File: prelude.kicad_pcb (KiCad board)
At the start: 2 copper layers, 80 x 60 mm, 41 parts, among them J1 CONN_01X50, J2 USB_C, J3 Conn_01x04, J4 Conn_01x08, SW1 SW_Push, U1 LM3671MF-3.3, U2 STM32F411RETx, U3 AP5724, Y1 16MHz

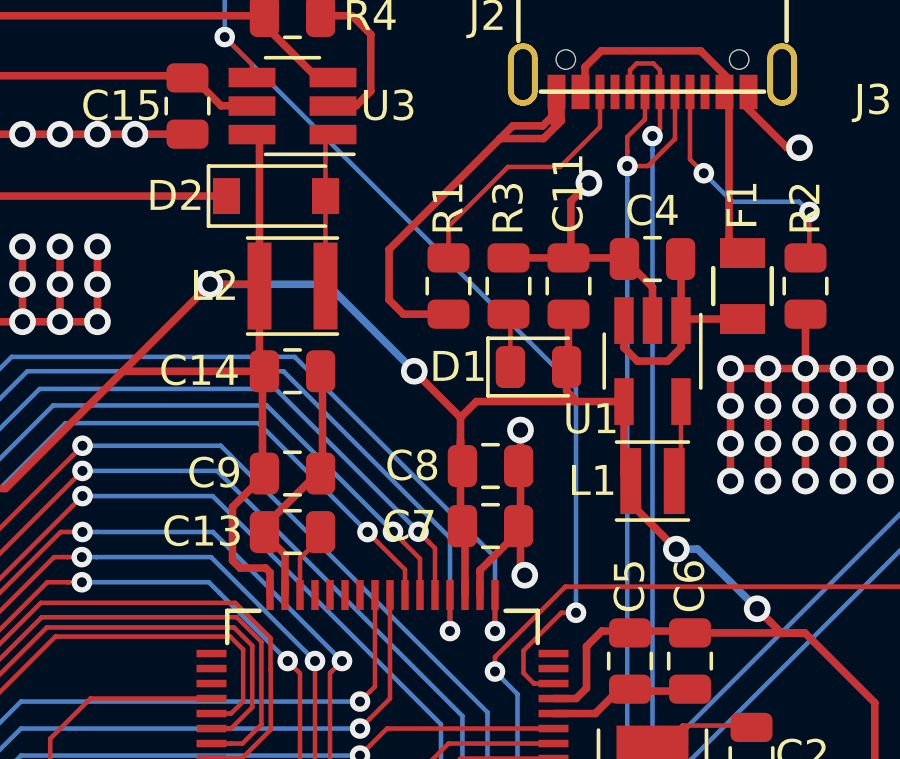
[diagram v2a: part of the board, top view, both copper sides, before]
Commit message: Replaces inductors with HandSoldering versions, recalculated fills, still need to adjust vias
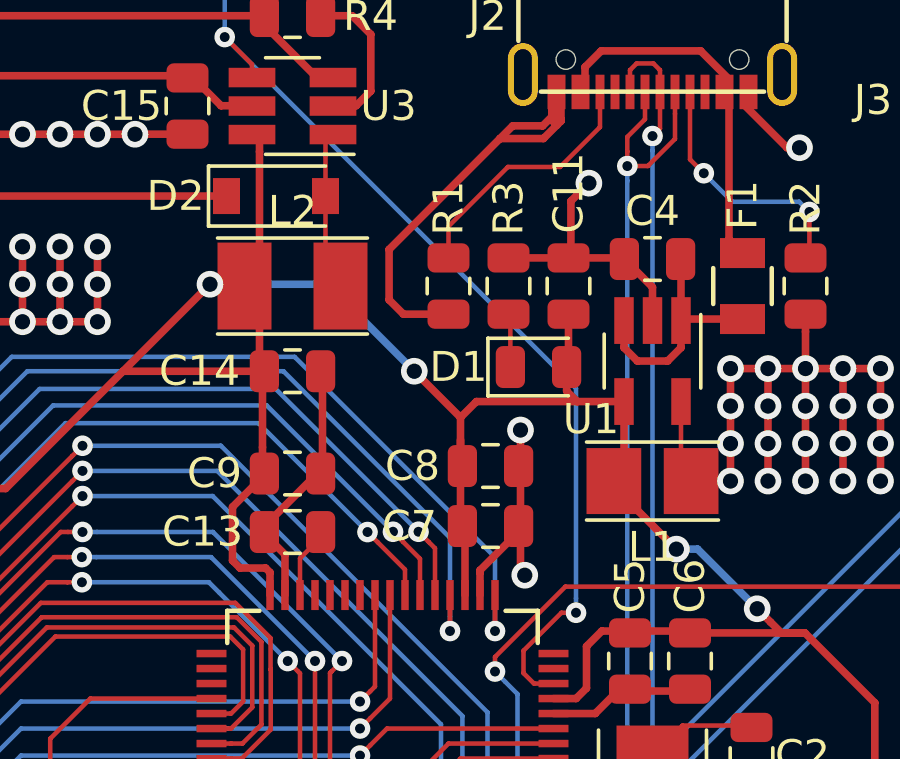
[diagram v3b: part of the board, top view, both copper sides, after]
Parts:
- L1: footprint Inductor_SMD:L_Taiyo-Yuden_NR-24xx -> Inductor_SMD:L_Taiyo-Yuden_NR-24xx_HandSoldering
- L2: footprint Inductor_SMD:L_Taiyo-Yuden_NR-30xx -> Inductor_SMD:L_Taiyo-Yuden_NR-30xx_HandSoldering
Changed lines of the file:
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@@
-    )
-  )
-  (module Inductor_SMD:L_Taiyo-Yuden_NR-24xx (layer Top)
-    (at 175 60.5 180)
-    (descr "Inductor, Taiyo Yuden, NR series, Taiyo-Yuden_NR-24xx, 2.4mmx2.4mm")
-    (tags "inductor taiyo-yuden nr smd")
-    (attr smd)
-    (fp_text reference L1 (at 2 0 180) (layer F.SilkS)
-      (effects (font (size 1 1) (thickness 0.15)))
-    )
-    (fp_text value 2.2uH (at 0 2.7 180) (layer F.Fab)
-      (effects (font (size 1 1) (thickness 0.15)))
-    )
-    (fp_text user %R (at 0 0 180) (layer F.Fab)
-      (effects (font (size 0.5 0.5) (thickness 0.075)))
-    )
-    (fp_line (start -1.2 0) (end -1.2 -0.725) (layer F.Fab) (width 0.1))
-    (fp_line (start -1.2 -0.725) (end -0.725 -1.2) (layer F.Fab) (width 0.1))
-    (fp_line (start -0.725 -1.2) (end 0 -1.2) (layer F.Fab) (width 0.1))
-    (fp_line (start 1.2 0) (end 1.2 -0.725) (layer F.Fab) (width 0.1))
-    (fp_line (start 1.2 -0.725) (end 0.725 -1.2) (layer F.Fab) (width 0.1))
-    (fp_line (start 0.725 -1.2) (end 0 -1.2) (layer F.Fab) (width 0.1))
-    (fp_line (start 1.2 0) (end 1.2 0.725) (layer F.Fab) (width 0.1))
-    (fp_line (start 1.2 0.725) (end 0.725 1.2) (layer F.Fab) (width 0.1))
-    (fp_line (start 0.725 1.2) (end 0 1.2) (layer F.Fab) (width 0.1))
-    (fp_line (start -1.2 0) (end -1.2 0.725) (layer F.Fab) (width 0.1))
-    (fp_line (start -1.2 0.725) (end -0.725 1.2) (layer F.Fab) (width 0.1))
-    (fp_line (start -0.725 1.2) (end 0 1.2) (layer F.Fab) (width 0.1))
-    (fp_line (start -1.2 -1.3) (end 1.2 -1.3) (layer F.SilkS) (width 0.12))
-    (fp_line (start -1.2 1.3) (end 1.2 1.3) (layer F.SilkS) (width 0.12))
-    (fp_line (start -1.5 -1.5) (end -1.5 1.5) (layer F.CrtYd) (width 0.05))
-    (fp_line (start -1.5 1.5) (end 1.5 1.5) (layer F.CrtYd) (width 0.05))
-    (fp_line (start 1.5 1.5) (end 1.5 -1.5) (layer F.CrtYd) (width 0.05))
-    (fp_line (start 1.5 -1.5) (end -1.5 -1.5) (layer F.CrtYd) (width 0.05))
-    (pad 1 smd rect (at -0.725 0 180) (size 0.7 2.2) (layers Top F.Paste F.Mask)
-      (net 36 "Net-(L1-Pad1)"))
-    (pad 2 smd rect (at 0.725 0 180) (size 0.7 2.2) (layers Top F.Paste F.Mask)
-      (net 5 +3V3))
-    (model ${KISYS3DMOD}/Inductor_SMD.3dshapes/L_Taiyo-Yuden_NR-24xx.wrl
-      (at (xyz 0 0 0))
-      (scale (xyz 1 1 1))
-      (rotate (xyz 0 0 0))
-    )
-    (model C:/Github/3DModels/Inductor_Taiyo_Yuden_NR2412_original.step
-      (at (xyz 0 0 0))
-      (scale (xyz 1 1 1))
-      (rotate (xyz 0 0 0))
-    )
-  )
-  (module Inductor_SMD:L_Taiyo-Yuden_NR-30xx (layer Top)
-    (at 163 54)
-    (descr "Inductor, Taiyo Yuden, NR series, Taiyo-Yuden_NR-30xx, 3.0mmx3.0mm")
-    (tags "inductor taiyo-yuden nr smd")
-    (attr smd)
-    (fp_text reference L2 (at -2.6 0 180) (layer F.SilkS)
-      (effects (font (size 1 1) (thickness 0.15)))
-    )
-    (fp_text value 22uH (at 0 3) (layer F.Fab)
-      (effects (font (size 1 1) (thickness 0.15)))
-    )
-    (fp_text user %R (at 0 0) (layer F.Fab)
-      (effects (font (size 0.7 0.7) (thickness 0.105)))
-    )
-    (fp_line (start -1.5 0) (end -1.5 -0.95) (layer F.Fab) (width 0.1))
-    (fp_line (start -1.5 -0.95) (end -0.95 -1.5) (layer F.Fab) (width 0.1))
-    (fp_line (start -0.95 -1.5) (end 0 -1.5) (layer F.Fab) (width 0.1))
-    (fp_line (start 1.5 0) (end 1.5 -0.95) (layer F.Fab) (width 0.1))
-    (fp_line (start 1.5 -0.95) (end 0.95 -1.5) (layer F.Fab) (width 0.1))
-    (fp_line (start 0.95 -1.5) (end 0 -1.5) (layer F.Fab) (width 0.1))
-    (fp_line (start 1.5 0) (end 1.5 0.95) (layer F.Fab) (width 0.1))
-    (fp_line (start 1.5 0.95) (end 0.95 1.5) (layer F.Fab) (width 0.1))
-    (fp_line (start 0.95 1.5) (end 0 1.5) (layer F.Fab) (width 0.1))
-    (fp_line (start -1.5 0) (end -1.5 0.95) (layer F.Fab) (width 0.1))
-    (fp_line (start -1.5 0.95) (end -0.95 1.5) (layer F.Fab) (width 0.1))
-    (fp_line (start -0.95 1.5) (end 0 1.5) (layer F.Fab) (width 0.1))
-    (fp_line (start -1.5 -1.6) (end 1.5 -1.6) (layer F.SilkS) (width 0.12))
-    (fp_line (start -1.5 1.6) (end 1.5 1.6) (layer F.SilkS) (width 0.12))
-    (fp_line (start -1.8 -1.8) (end -1.8 1.8) (layer F.CrtYd) (width 0.05))
-    (fp_line (start -1.8 1.8) (end 1.8 1.8) (layer F.CrtYd) (width 0.05))
-    (fp_line (start 1.8 1.8) (end 1.8 -1.8) (layer F.CrtYd) (width 0.05))
-    (fp_line (start 1.8 -1.8) (end -1.8 -1.8) (layer F.CrtYd) (width 0.05))
-    (pad 1 smd rect (at -1.1 0) (size 0.8 2.9) (layers Top F.Paste F.Mask)
-      (net 5 +3V3))
-    (pad 2 smd rect (at 1.1 0) (size 0.8 2.9) (layers Top F.Paste F.Mask)
-      (net 8 "Net-(D2-Pad2)"))
-    (model ${KISYS3DMOD}/Inductor_SMD.3dshapes/L_Taiyo-Yuden_NR-30xx.wrl
-      (at (xyz 0 0 0))
-      (scale (xyz 1 1 1))
-      (rotate (xyz 0 0 0))
-    )
-    (model C:/Github/3DModels/Inductor_Taiyo_Yuden_NR3015_original.step
-      (at (xyz 0 0 0))
-      (scale (xyz 1 1 1))
-      (rotate (xyz 0 0 0))
     )
   )
@@
       (at (xyz 0 0 0))
       (scale (xyz 1 1 1))
+      (rotate (xyz 0 0 0))
+    )
+  )
+  (module Inductor_SMD:L_Taiyo-Yuden_NR-24xx_HandSoldering (layer Top)
+    (at 175 60.5 180)
+    (descr "Inductor, Taiyo Yuden, NR series, Taiyo-Yuden_NR-24xx, 2.4mmx2.4mm")
+    (tags "inductor taiyo-yuden nr smd")
+    (attr smd)
+    (fp_text reference L1 (at 0 -2.2 180) (layer F.SilkS)
+      (effects (font (size 1 1) (thickness 0.15)))
+    )
+    (fp_text value 2.2uH (at 0 2.7 180) (layer F.Fab)
+      (effects (font (size 1 1) (thickness 0.15)))
+    )
+    (fp_text user %R (at 0 0 180) (layer F.Fab)
+      (effects (font (size 0.5 0.5) (thickness 0.075)))
+    )
+    (fp_line (start -1.2 0) (end -1.2 -0.725) (layer F.Fab) (width 0.1))
+    (fp_line (start -1.2 -0.725) (end -0.725 -1.2) (layer F.Fab) (width 0.1))
+    (fp_line (start -0.725 -1.2) (end 0 -1.2) (layer F.Fab) (width 0.1))
+    (fp_line (start 1.2 0) (end 1.2 -0.725) (layer F.Fab) (width 0.1))
+    (fp_line (start 1.2 -0.725) (end 0.725 -1.2) (layer F.Fab) (width 0.1))
+    (fp_line (start 0.725 -1.2) (end 0 -1.2) (layer F.Fab) (width 0.1))
+    (fp_line (start 1.2 0) (end 1.2 0.725) (layer F.Fab) (width 0.1))
+    (fp_line (start 1.2 0.725) (end 0.725 1.2) (layer F.Fab) (width 0.1))
+    (fp_line (start 0.725 1.2) (end 0 1.2) (layer F.Fab) (width 0.1))
+    (fp_line (start -1.2 0) (end -1.2 0.725) (layer F.Fab) (width 0.1))
+    (fp_line (start -1.2 0.725) (end -0.725 1.2) (layer F.Fab) (width 0.1))
+    (fp_line (start -0.725 1.2) (end 0 1.2) (layer F.Fab) (width 0.1))
+    (fp_line (start -2.2 -1.3) (end 2.2 -1.3) (layer F.SilkS) (width 0.12))
+    (fp_line (start -2.2 1.3) (end 2.2 1.3) (layer F.SilkS) (width 0.12))
+    (fp_line (start -2.5 -1.5) (end -2.5 1.5) (layer F.CrtYd) (width 0.05))
+    (fp_line (start -2.5 1.5) (end 2.5 1.5) (layer F.CrtYd) (width 0.05))
+    (fp_line (start 2.5 1.5) (end 2.5 -1.5) (layer F.CrtYd) (width 0.05))
+    (fp_line (start 2.5 -1.5) (end -2.5 -1.5) (layer F.CrtYd) (width 0.05))
+    (pad 1 smd rect (at -1.2875 0 180) (size 1.825 2.2) (layers Top F.Paste F.Mask)
+      (net 36 "Net-(L1-Pad1)"))
+    (pad 2 smd rect (at 1.2875 0 180) (size 1.825 2.2) (layers Top F.Paste F.Mask)
+      (net 5 +3V3))
+    (model ${KISYS3DMOD}/Inductor_SMD.3dshapes/L_Taiyo-Yuden_NR-24xx.wrl
+      (at (xyz 0 0 0))
+      (scale (xyz 1 1 1))
+      (rotate (xyz 0 0 0))
+    )
+  )
+  (module Inductor_SMD:L_Taiyo-Yuden_NR-30xx_HandSoldering (layer Top)
+    (at 163 54)
+    (descr "Inductor, Taiyo Yuden, NR series, Taiyo-Yuden_NR-30xx, 3.0mmx3.0mm")
+    (tags "inductor taiyo-yuden nr smd")
+    (attr smd)
+    (fp_text reference L2 (at 0 -2.5) (layer F.SilkS)
+      (effects (font (size 1 1) (thickness 0.15)))
+    )
+    (fp_text value 22uH (at 0 3) (layer F.Fab)
+      (effects (font (size 1 1) (thickness 0.15)))
+    )
+    (fp_text user %R (at 0 0) (layer F.Fab)
+      (effects (font (size 0.7 0.7) (thickness 0.105)))
+    )
+    (fp_line (start -1.5 0) (end -1.5 -0.95) (layer F.Fab) (width 0.1))
+    (fp_line (start -1.5 -0.95) (end -0.95 -1.5) (layer F.Fab) (width 0.1))
+    (fp_line (start -0.95 -1.5) (end 0 -1.5) (layer F.Fab) (width 0.1))
+    (fp_line (start 1.5 0) (end 1.5 -0.95) (layer F.Fab) (width 0.1))
+    (fp_line (start 1.5 -0.95) (end 0.95 -1.5) (layer F.Fab) (width 0.1))
+    (fp_line (start 0.95 -1.5) (end 0 -1.5) (layer F.Fab) (width 0.1))
+    (fp_line (start 1.5 0) (end 1.5 0.95) (layer F.Fab) (width 0.1))
+    (fp_line (start 1.5 0.95) (end 0.95 1.5) (layer F.Fab) (width 0.1))
+    (fp_line (start 0.95 1.5) (end 0 1.5) (layer F.Fab) (width 0.1))
+    (fp_line (start -1.5 0) (end -1.5 0.95) (layer F.Fab) (width 0.1))
+    (fp_line (start -1.5 0.95) (end -0.95 1.5) (layer F.Fab) (width 0.1))
+    (fp_line (start -0.95 1.5) (end 0 1.5) (layer F.Fab) (width 0.1))
+    (fp_line (start -2.5 -1.6) (end 2.5 -1.6) (layer F.SilkS) (width 0.12))
+    (fp_line (start -2.5 1.6) (end 2.5 1.6) (layer F.SilkS) (width 0.12))
+    (fp_line (start -2.75 -1.8) (end -2.75 1.8) (layer F.CrtYd) (width 0.05))
+    (fp_line (start -2.75 1.8) (end 2.75 1.8) (layer F.CrtYd) (width 0.05))
+    (fp_line (start 2.75 1.8) (end 2.75 -1.8) (layer F.CrtYd) (width 0.05))
+    (fp_line (start 2.75 -1.8) (end -2.75 -1.8) (layer F.CrtYd) (width 0.05))
+    (pad 1 smd rect (at -1.6 0) (size 1.8 2.9) (layers Top F.Paste F.Mask)
+      (net 5 +3V3))
+    (pad 2 smd rect (at 1.6 0) (size 1.8 2.9) (layers Top F.Paste F.Mask)
+      (net 8 "Net-(D2-Pad2)"))
+    (model ${KISYS3DMOD}/Inductor_SMD.3dshapes/L_Taiyo-Yuden_NR-30xx.wrl
+      (at (xyz 0 0 0))
+      (scale (xyz 1 1 1))

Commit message: Adjusted vias and tracks with latest Inductor footprints (HandSoldering), removed row of vias
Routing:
- net GND: track 350.2 -> 345.2 mm, vias 224 -> 220
- net +3V3: track 206.7 -> 207.8 mm
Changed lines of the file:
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@@
     (thickness 1.6)
     (drawings 24)
-    (tracks 1102)
+    (tracks 1099)
     (zones 0)
     (modules 41)
@@
   (via (at 180.1 56.75) (size 0.889) (drill 0.508) (layers Top Bottom) (net 2))
   (via (at 178.85 56.75) (size 0.889) (drill 0.508) (layers Top Bottom) (net 2))
-  (via (at 177.6 56.75) (size 0.889) (drill 0.508) (layers Top Bottom) (net 2))
   (via (at 178.85 58) (size 0.889) (drill 0.508) (layers Top Bottom) (net 2))
-  (via (at 177.6 58) (size 0.889) (drill 0.508) (layers Top Bottom) (net 2))
   (via (at 178.85 59.25) (size 0.889) (drill 0.508) (layers Top Bottom) (net 2))
-  (via (at 177.6 59.25) (size 0.889) (drill 0.508) (layers Top Bottom) (net 2))
   (via (at 178.85 60.5) (size 0.889) (drill 0.508) (layers Top Bottom) (net 2))
-  (via (at 177.6 60.5) (size 0.889) (drill 0.508) (layers Top Bottom) (net 2))
   (via (at 181.35 56.75) (size 0.889) (drill 0.508) (layers Top Bottom) (net 2))
-  (via (at 182.6 56.75) (size 0.889) (drill 0.508) (layers Top Bottom) (net 2))
   (via (at 180.1 58) (size 0.889) (drill 0.508) (layers Top Bottom) (net 2))
   (via (at 181.35 58) (size 0.889) (drill 0.508) (layers Top Bottom) (net 2))
-  (via (at 182.6 58) (size 0.889) (drill 0.508) (layers Top Bottom) (net 2))
   (via (at 180.1 59.25) (size 0.889) (drill 0.508) (layers Top Bottom) (net 2))
   (via (at 181.35 59.25) (size 0.889) (drill 0.508) (layers Top Bottom) (net 2))
-  (via (at 182.6 59.25) (size 0.889) (drill 0.508) (layers Top Bottom) (net 2))
   (via (at 180.1 60.5) (size 0.889) (drill 0.508) (layers Top Bottom) (net 2))
   (via (at 181.35 60.5) (size 0.889) (drill 0.508) (layers Top Bottom) (net 2))
-  (via (at 182.6 60.5) (size 0.889) (drill 0.508) (layers Top Bottom) (net 2))
   (segment (start 149.732222 59.75) (end 148.865 59.75) (width 0.254) (layer Top) (net 2))
   (segment (start 150.25 55.19) (end 150.25 59.232222) (width 0.254) (layer Top) (net 2))
@@
   (segment (start 149 52.69) (end 149 53.94) (width 0.254) (layer Top) (net 2))
   (segment (start 149 53.94) (end 149 55.19) (width 0.254) (layer Top) (net 2))
-  (segment (start 178.85 56.75) (end 177.6 56.75) (width 0.254) (layer Top) (net 2))
   (segment (start 178.85 56.75) (end 180.1 56.75) (width 0.254) (layer Top) (net 2))
   (segment (start 180.1 56.75) (end 181.35 56.75) (width 0.254) (layer Top) (net 2))
-  (segment (start 181.35 56.75) (end 182.6 56.75) (width 0.254) (layer Top) (net 2))
-  (segment (start 182.6 56.75) (end 182.6 58) (width 0.254) (layer Top) (net 2))
   (segment (start 181.35 56.75) (end 181.35 58) (width 0.254) (layer Top) (net 2))
   (segment (start 181.35 58) (end 181.35 59.25) (width 0.254) (layer Top) (net 2))
@@
   (segment (start 178.85 58) (end 178.85 59.25) (width 0.254) (layer Top) (net 2))
   (segment (start 178.85 59.25) (end 178.85 60.5) (width 0.254) (layer Top) (net 2))
-  (segment (start 177.6 56.75) (end 177.6 58) (width 0.254) (layer Top) (net 2))
-  (segment (start 177.6 58) (end 177.6 59.25) (width 0.254) (layer Top) (net 2))
-  (segment (start 177.6 59.25) (end 177.6 60.5) (width 0.254) (layer Top) (net 2))
-  (segment (start 182.6 58) (end 182.6 59.25) (width 0.254) (layer Top) (net 2))
-  (segment (start 182.6 59.25) (end 182.6 60.5) (width 0.254) (layer Top) (net 2))
   (via (at 180.2975 71.8375) (size 0.889) (drill 0.508) (layers Top Bottom) (net 2))
   (segment (start 180.2975 71.8375) (end 180.2975 70.5875) (width 0.254) (layer Top) (net 2))
@@
   (segment (start 170.4 85.7) (end 170.4 86.654) (width 0.254) (layer Top) (net 2))
   (segment (start 170.4 86.654) (end 170.796 87.05) (width 0.254) (layer Top) (net 2))
+  (segment (start 182.6 59.25) (end 182.6 60.5) (width 0.254) (layer Top) (net 2))
+  (segment (start 181.35 56.75) (end 182.6 56.75) (width 0.254) (layer Top) (net 2))
+  (segment (start 182.6 58) (end 182.6 59.25) (width 0.254) (layer Top) (net 2))
+  (segment (start 182.6 56.75) (end 182.6 58) (width 0.254) (layer Top) (net 2))
+  (via (at 182.6 59.25) (size 0.889) (drill 0.508) (layers Top Bottom) (net 2))
+  (via (at 182.6 60.5) (size 0.889) (drill 0.508) (layers Top Bottom) (net 2))
+  (via (at 182.6 58) (size 0.889) (drill 0.508) (layers Top Bottom) (net 2))
+  (via (at 182.6 56.75) (size 0.889) (drill 0.508) (layers Top Bottom) (net 2))
   (segment (start 178 68.65) (end 176 68.65) (width 0.1524) (layer Top) (net 3))
   (segment (start 176 68.65) (end 175 69.65) (width 0.1524) (layer Top) (net 3))
@@
   (segment (start 174.05 60.275) (end 174.275 60.5) (width 0.254) (layer Top) (net 5))
   (segment (start 174.05 57.85) (end 174.05 60.275) (width 0.254) (layer Top) (net 5))
-  (segment (start 164.16 53.94) (end 167.06 56.84) (width 0.254) (layer Bottom) (net 5))
-  (via (at 160.25 53.94) (size 0.889) (drill 0.508) (layers Top Bottom) (net 5))
-  (segment (start 153.44 60.75) (end 160.25 53.94) (width 0.254) (layer Top) (net 5))
-  (segment (start 148.865 60.75) (end 153.44 60.75) (width 0.254) (layer Top) (net 5))
-  (segment (start 157.35 56.84) (end 161.98 56.84) (width 0.254) (layer Top) (net 5))
-  (segment (start 161.84 53.94) (end 161.9 54) (width 0.254) (layer Top) (net 5))
-  (segment (start 160.25 53.94) (end 161.84 53.94) (width 0.254) (layer Top) (net 5))
-  (segment (start 160.25 53.94) (end 164.16 53.94) (width 0.254) (layer Bottom) (net 5))
   (segment (start 180.0825 65.5625) (end 179.29589 65.5625) (width 0.254) (layer Top) (net 5))
   (segment (start 179.29589 65.5625) (end 178.934499 65.201109) (width 0.254) (layer Top) (net 5))
@@
   (segment (start 156.578 97.028) (end 152.384 92.834) (width 0.254) (layer Top) (net 5))
   (segment (start 152.384 92.834) (end 152.384 84.696) (width 0.254) (layer Top) (net 5))
+  (via (at 159.749952 53.94) (size 0.889) (drill 0.508) (layers Top Bottom) (net 5))
+  (segment (start 160.378569 53.94) (end 159.749952 53.94) (width 0.254) (layer Top) (net 5))
+  (segment (start 161.9 54) (end 161.84 53.94) (width 0.254) (layer Top) (net 5))
+  (segment (start 161.84 53.94) (end 160.378569 53.94) (width 0.254) (layer Top) (net 5))
+  (segment (start 160.378569 53.94) (end 159.749952 53.94) (width 0.254) (layer Bottom) (net 5))
+  (segment (start 164.16 53.94) (end 160.378569 53.94) (width 0.254) (layer Bottom) (net 5))
+  (segment (start 167.06 56.84) (end 164.16 53.94) (width 0.254) (layer Bottom) (net 5))
+  (segment (start 152.939952 60.75) (end 148.865 60.75) (width 0.254) (layer Top) (net 5))
+  (segment (start 161.470024 56.844976) (end 156.844976 56.844976) (width 0.254) (layer Top) (net 5))
+  (segment (start 161.475 56.84) (end 161.470024 56.844976) (width 0.254) (layer Top) (net 5))
+  (segment (start 162.0625 56.84) (end 161.475 56.84) (width 0.254) (layer Top) (net 5))
+  (segment (start 159.749952 53.94) (end 156.844976 56.844976) (width 0.254) (layer Top) (net 5))
+  (segment (start 156.844976 56.844976) (end 152.939952 60.75) (width 0.254) (layer Top) (net 5))
   (segment (start 160.618824 47.99) (end 160.97 47.99) (width 0.254) (layer Top) (net 6))
   (segment (start 159.618824 46.99) (end 160.618824 47.99) (width 0.254) (layer Top) (net 6))
